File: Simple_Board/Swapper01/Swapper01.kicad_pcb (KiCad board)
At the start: 2 copper layers, 83 x 38 mm, 35 parts, among them J1 DB9_Female_MountingHoles

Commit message: Upddate
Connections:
- J1 pad 4: /V+_2 -> /I+_2
- J1 pad 5: /V-_2 -> /I-_2
- J1 pad 8: /I+_2 -> /V+_2
- J1 pad 9: /I-_2 -> /V-_2
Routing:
- net /V-_2: track 7.77 -> 11.5 mm
- net /V+_2: track 15.3 -> 18.8 mm
- net /I-_2: track 9.09 -> 6.99 mm
- net /I+_2: track 10.8 -> 11.9 mm
- net /V-: track 18.4 -> 18.5 mm, vias 0 -> 1

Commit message: Update
Nearly finished versions of simple and Calibrator board
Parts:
- added J2: Conn_01x04, Connector_JST:JST_SH_SM04B-SRSS-TB_1x04-1MP_P1.00mm_Horizontal, F.Cu at (8.26, -22.2)
- J1: footprint Connector:DB9_ASSMANN -> 0_Swapper01:DSUB-TH_DMR-9S
- moved J1 6.84 mm to (-2.54, -6.35), turned to 180 degrees
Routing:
- net /V_in: track 65.8 -> 112.2 mm
- net /I_in: track 73.0 -> 95.0 mm, vias 6 -> 10
- net /I_out: track 72.0 -> 83.3 mm, vias 6 -> 7
- net /V_out: track 65.9 -> 73.7 mm
- net /V-: track 18.5 -> 15.0 mm
- net /V-_2: track 11.5 -> 13.0 mm
- net /I-_2: track 6.99 -> 8.50 mm
- net /I-: track 10.1 -> 11.6 mm
- net /I+: track 6.74 -> 8.20 mm
- net /V+: track 11.8 -> 13.3 mm
- net /I+_2: track 11.9 -> 12.8 mm
- net /V+_2: track 18.8 -> 19.5 mm

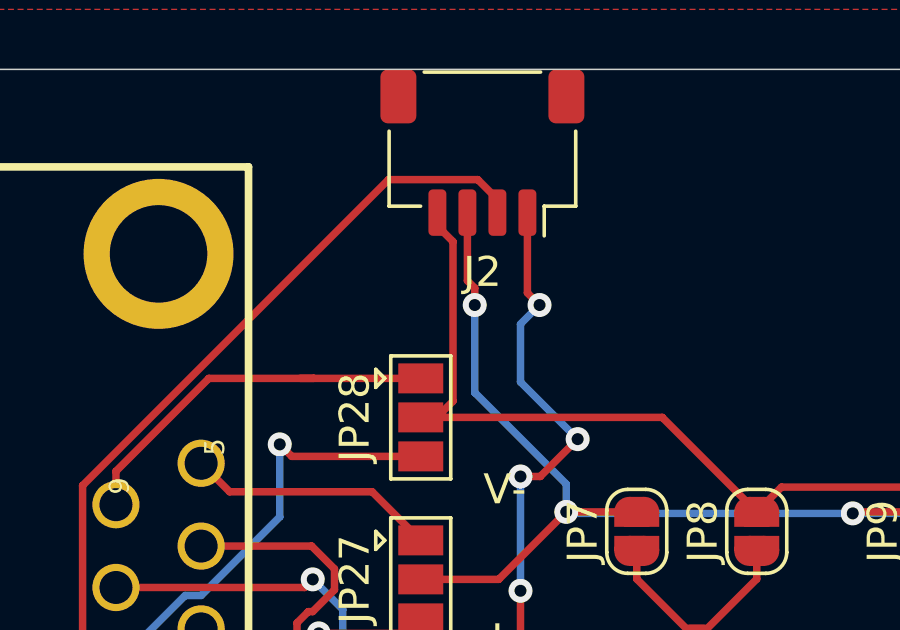
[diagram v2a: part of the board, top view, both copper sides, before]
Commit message: Fixed jst pinouts and made Cali board
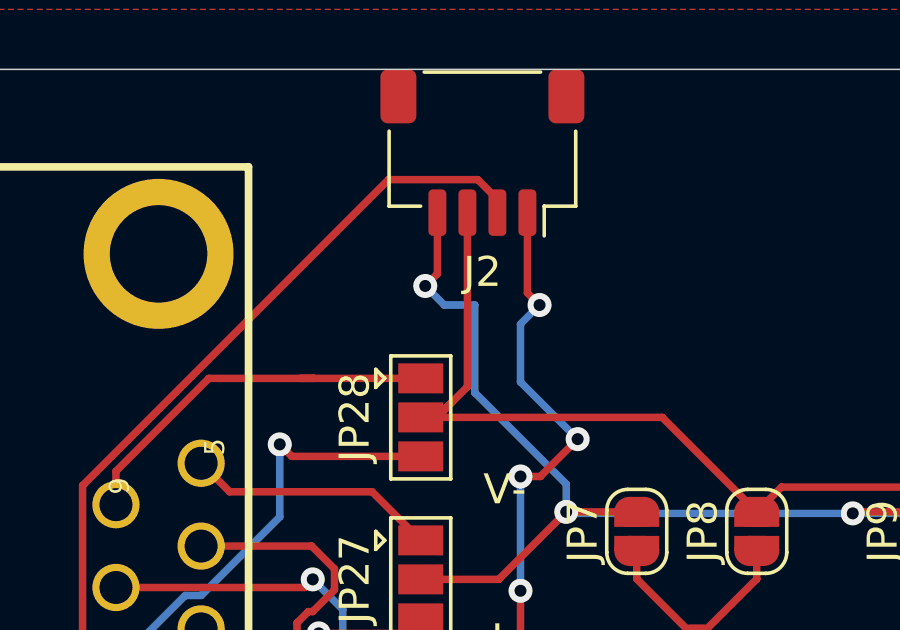
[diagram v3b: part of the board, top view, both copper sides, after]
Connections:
- J2 pad 3: /I_out -> /V_out
- J2 pad 4: /V_out -> /I_out
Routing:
- net /I_out: track 83.3 -> 85.1 mm
- net /V_out: track 73.7 -> 74.5 mm

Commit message: Update
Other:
- board text added: "Swapper_01 Ryan Morgenstern 5/16/2022"
